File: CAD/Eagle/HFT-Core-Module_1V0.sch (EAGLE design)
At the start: 315 parts, among them Q0521 ABS07-32.768KHZ, Q0911 ABM3B-16MHZ-10-R50-1-U, U0111 STM32L4Z_144PIN_SMPS, U0431 PAM2305AAB120, U0601 LM4120IM5-3.0, U0611 MAX5217, U0631 CFPT-141-20MHZ, U0641 OPA354, U0701 SI5338, U0801 NHD-C0220BIZ_2X20CHARS, U0901 AX5243, U1001 AX5243, U1101 MCP3911A0-E-SS, U1111 MAX5136AGTG+, U1121 OPA354, U1131 OPA354, U1141 OPA354, U1601 SOLARPANEL_3V3_5MA1_25MM_X_20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, U1602 SPV1040T, U1701 TS5A23166, U1801 PAM2305AAB330, U1901 TS5A23166, U2001 TS5A23166, U2101 TS5A23166, X1401 SMA_SMT_AMPHENOL-901-143, X1411 SMA_SMT_AMPHENOL-901-143, X1501 CUI SJ1-3535NS, X1511 CUI SJ1-3535NS, X511 2X20/90_1MM27_HARWIN_M50-3202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, X512 2X20/90_1MM27_HARWIN_M50-3202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, X521 2X20/90_1MM27_HARWIN_M50-3202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, X522 2X20/90_1MM27_HARWIN_M50-3202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, X531 2X20/90_1MM27_HARWIN_M50-3202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, X532 2X20/90_1MM27_HARWIN_M50-3202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

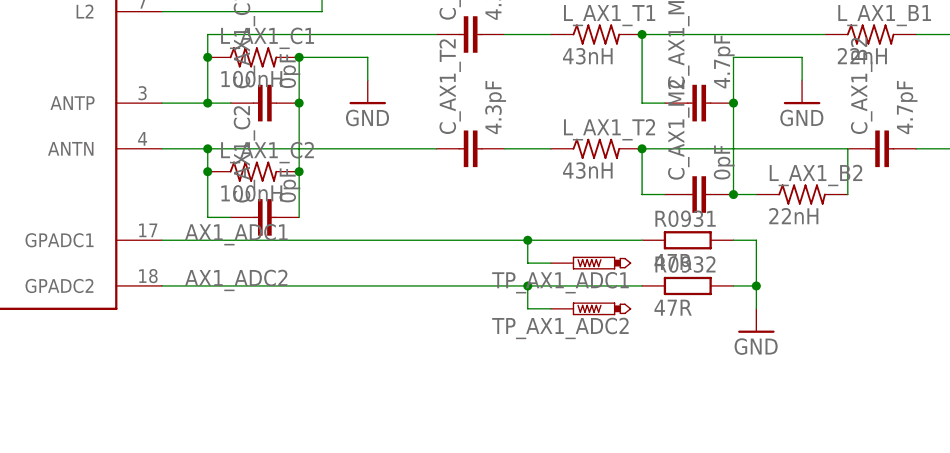
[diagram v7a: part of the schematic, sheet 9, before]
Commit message: HW_1V0 - minor fixes in schematics done
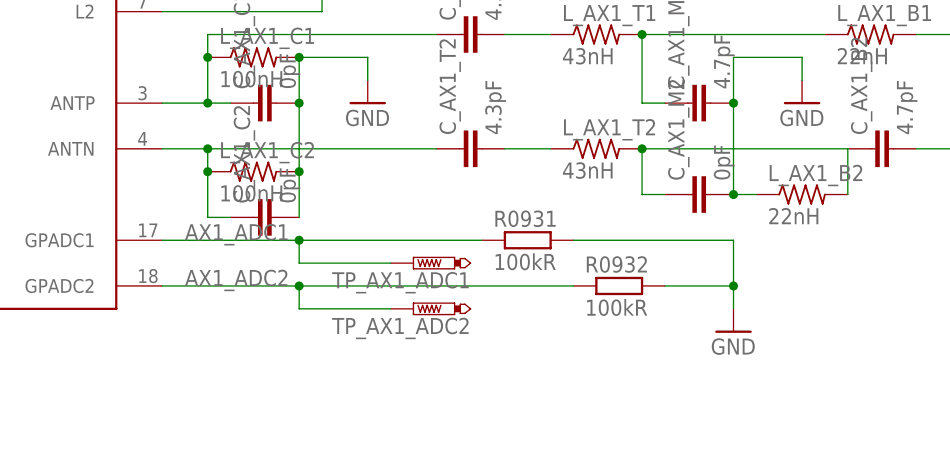
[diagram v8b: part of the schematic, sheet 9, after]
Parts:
- added R0841, R1110, R1702, R1902, R2002, R2102: 33kR, rcl:R-EU_R0603
- R0931, R0932, R1031, R1032: value 47R -> 100kR
- renumbered C1902 to C1903, C2002 to C2003, C2102 to C2103
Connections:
- net GND: now also R0841.1, R1110.1, R1702.1, R1902.1, R2002.1, R2102.1
- net MCU_20MHZ_EN: now also R1902.2
- net MCU_HICUR_EN: now also R2002.2
- net MCU_LCD_!RST: now also R0841.2
- net MCU_SPI1_AUDIO_ADC_!RESET: now also R1110.2
- net MCU_VDD12_EN: now also R2102.2
- net MCU_VUSB_EN: now also R1702.2; no longer C1701.1
- net VDDUSB: now also C1701.1
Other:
- note added: "Imax disabled"
- note added: "Rotary Encoder with Pushbutton"
- moved on the sheet: C0811, C0821, C0831, C1701, PF1311, R0931, R0932, R1031, R1032, TP_AX1_ADC1, TP_AX1_ADC2, TP_AX2_ADC1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
